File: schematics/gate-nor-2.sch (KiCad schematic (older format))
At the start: 4 parts, among them Q1 NPN

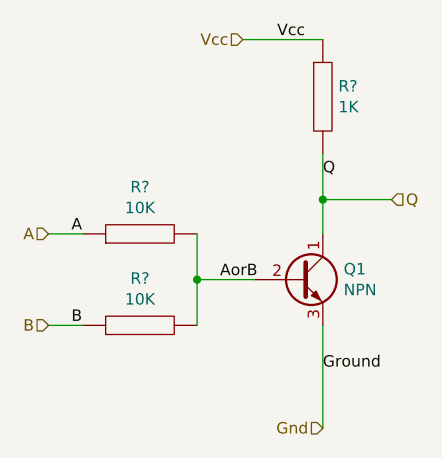
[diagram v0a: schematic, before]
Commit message: Adds ALU Schematics (#1)
* Adds a test for the 4-4-1 multiplexer
* Adds an xor gate
* Updates gitignore to include common swap files and data output
* Adds a four bit bitwise inverter
* Adds a one bit buffer
* Adds a 1->4 bit replicator
* Adds a 4 bit and gate
* ALU is sketched but has functional defects
* Adds a netlist "optimizer" which shortens names for better output parsing
* Adds a simple spice runner
* Adds a model injector and an op test injector
* Basic unit test automation framework for async circuits
* Adds a primitive directory iterator
* Adds some tests for and-2, nor-2, nor-3
* More testing.  Trying to find defect in ALU
* ALU appears to work as expected
* Updates README, adds some ALU tests
* Updates the schematics' README
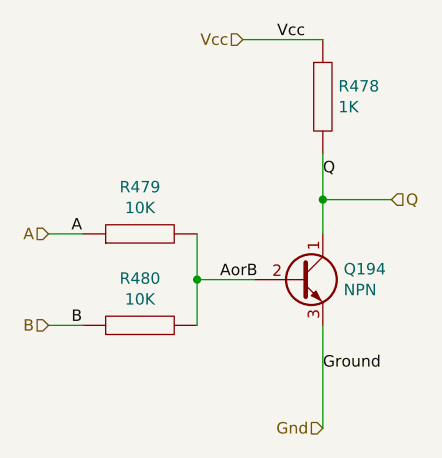
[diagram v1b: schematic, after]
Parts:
- removed Q1: NPN, Package_TO_SOT_THT:TO-92_Inline, symbol Transistor_BJT:BC548
- removed R3: 1K, symbol pspice:R
- added Q149: NPN, Package_TO_SOT_THT:TO-92_Inline, symbol Transistor_BJT:BC548
- added R349: 1K, symbol pspice:R
- renumbered R1 to R350, R2 to R351
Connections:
- net AorB: now also Q149.2 (B)
- net Gnd: now also Q149.3 (E)
- net Q: now also Q149.1 (C), R349.2
- net Vcc: now also R349.1
